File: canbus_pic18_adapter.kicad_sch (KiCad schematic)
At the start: 12 parts, among them J1 Conn_01x06_Socket, J2 Conn_01x14_Pin, J3 Conn_01x14_Pin, U1 PIC18F2XK80, Y1 10Mhz

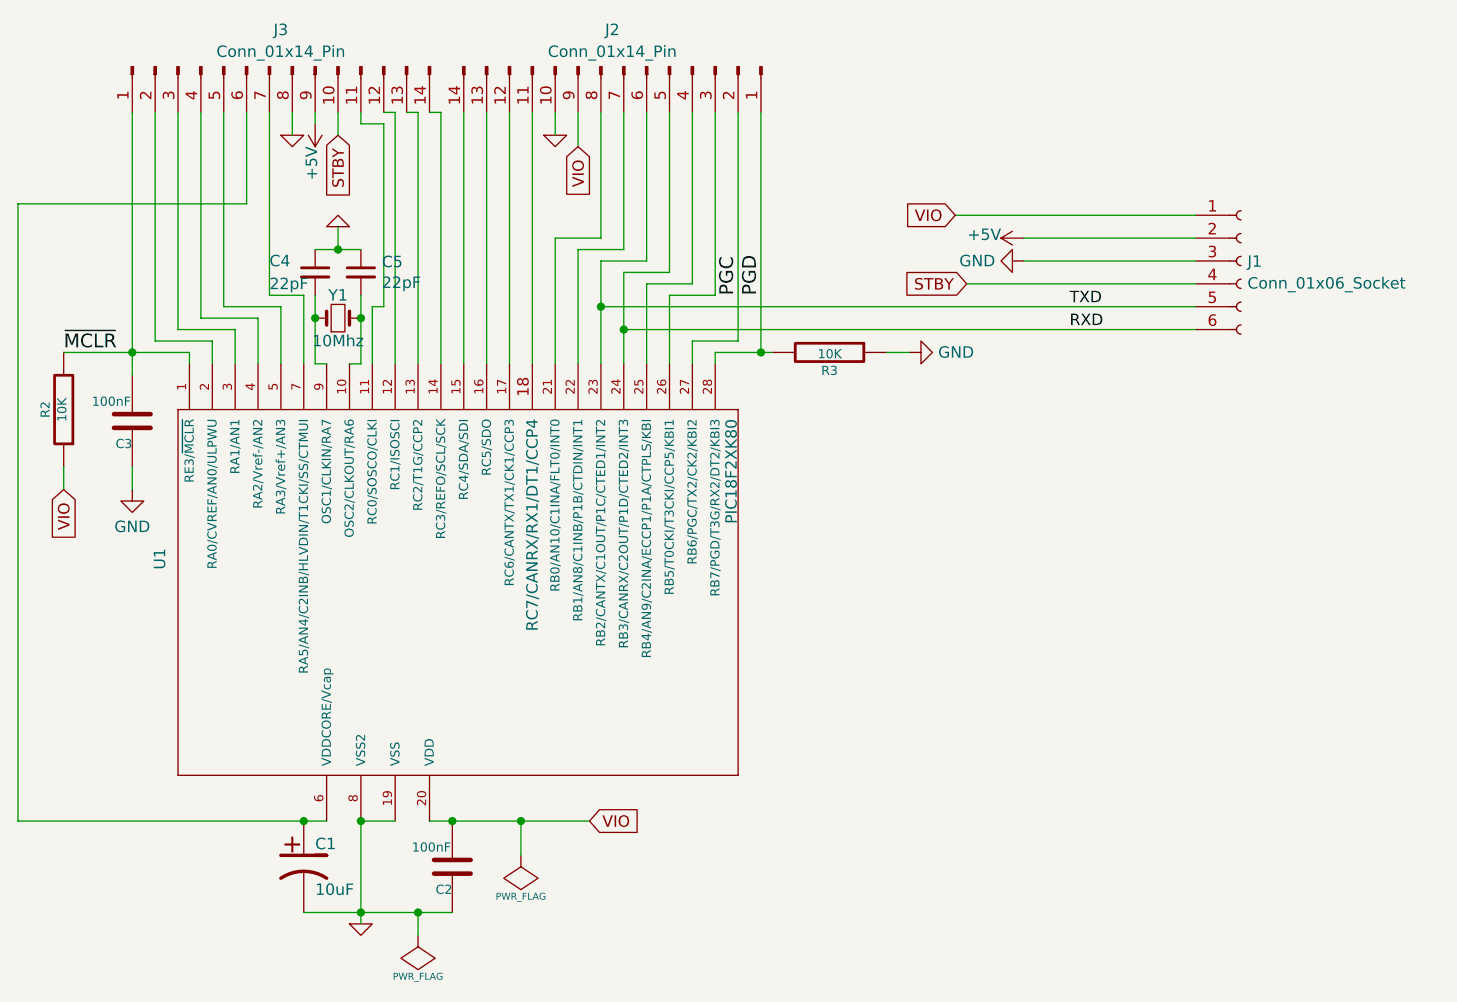
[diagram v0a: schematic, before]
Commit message: Add programming header Add a LED on VIO Other minor adjustemnts
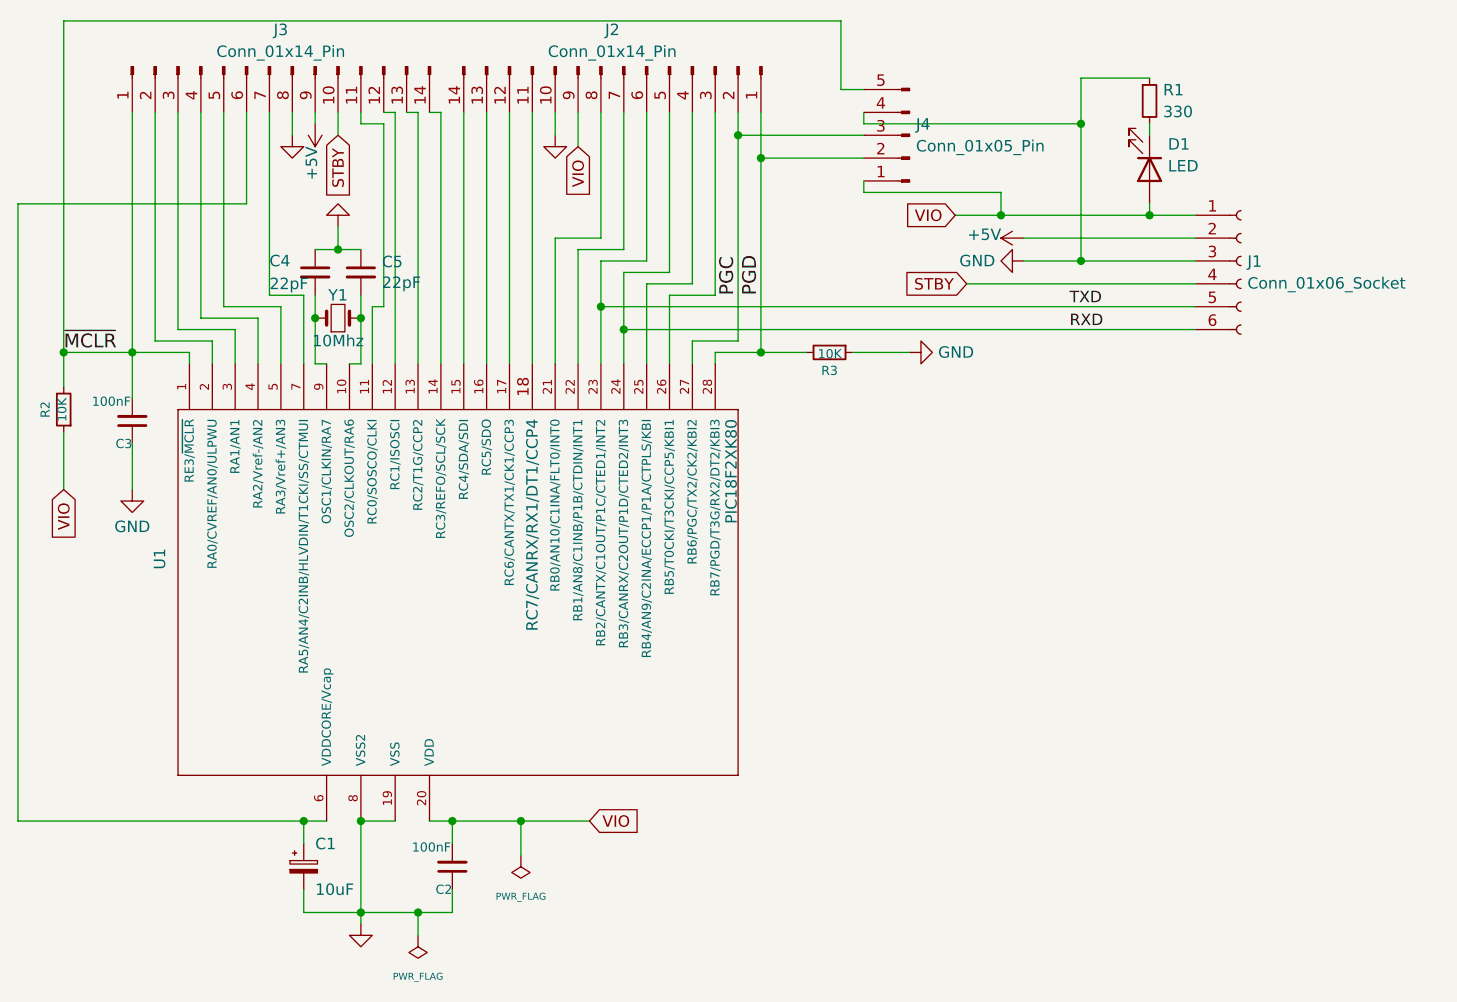
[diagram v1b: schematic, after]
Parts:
- added D1: LED, LED_THT:LED_D3.0mm, symbol Device:LED
- added J4: Conn_01x05_Pin, Connector_PinHeader_2.54mm:PinHeader_1x05_P2.54mm_Vertical, symbol Connector:Conn_01x05_Pin
- added R1: 330, Resistor_THT:R_Axial_DIN0309_L9.0mm_D3.2mm_P12.70mm_Horizontal, symbol Device:R_Small
- C1: footprint ~ -> Capacitor_SMD:C_0805_2012Metric_Pad1.18x1.45mm_HandSolder; symbol control-main-rescue:CP1-RESCUE-control-main -> Device:C_Polarized_Small
- C2, C3: footprint ~ -> Capacitor_SMD:C_0603_1608Metric_Pad1.08x0.95mm_HandSolder; symbol control-main-rescue:C-RESCUE-control-main -> Device:C_Small
- C4, C5: symbol remote-control-rescue:C_Small-Device-remote-control-rescue -> Device:C_Small
- J2, J3: footprint (none) -> Connector_PinHeader_2.54mm:PinHeader_1x14_P2.54mm_Vertical
- R2, R3: footprint ~ -> Resistor_SMD:R_0805_2012Metric_Pad1.20x1.40mm_HandSolder; symbol control-main-rescue:R-RESCUE-control-main -> Device:R_Small
- U1: footprint (none) -> Package_DIP:DIP-28_W7.62mm_Socket
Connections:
- net GND: now also J4.4 (Pin_4), R1.1
- net PGC: now also J4.3 (Pin_3)
- net PGD: now also J4.2 (Pin_2)
- net VIO: now also D1.2 (A), J4.1 (Pin_1)
- net ~{MCLR}: now also J4.5 (Pin_5)
- new net: D1.1 (K), R1.2
